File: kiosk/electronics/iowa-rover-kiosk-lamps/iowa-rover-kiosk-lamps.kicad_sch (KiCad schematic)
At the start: 12 parts, among them J1 Conn_01x08, SW1 SW_Push, U1 TPIC6A595NE

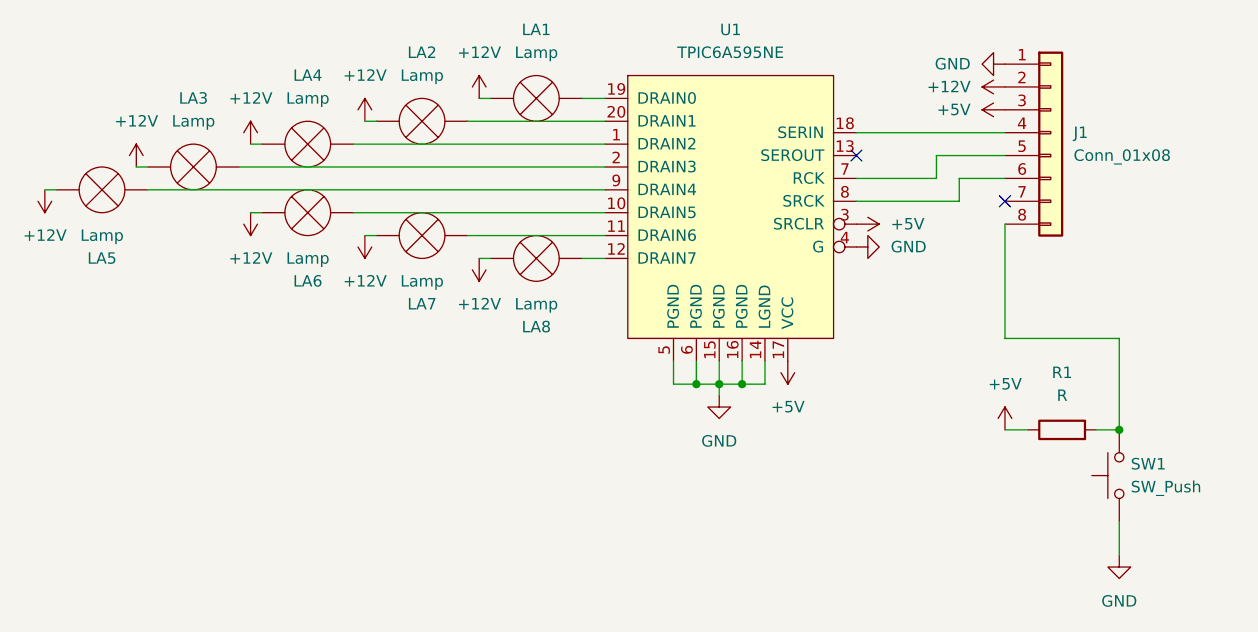
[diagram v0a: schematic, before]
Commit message: initial pass at board drawings
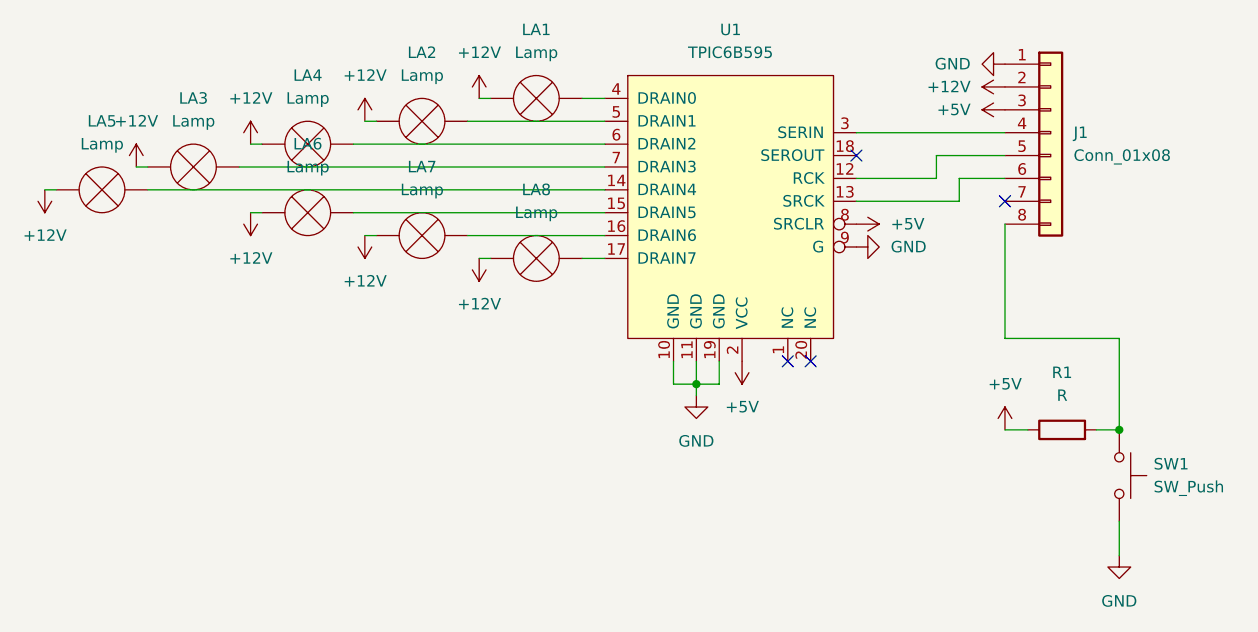
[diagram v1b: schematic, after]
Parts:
- removed U1: TPIC6A595NE, symbol SMM:TPIC6A595NE
- added U1: TPIC6B595, Package_DIP:DIP-20_W7.62mm_Socket, symbol SMM:TPIC6B595
- J1: footprint (none) -> Connector_PinHeader_2.54mm:PinHeader_2x04_P2.54mm_Vertical
- LA1, LA2, LA3, LA4, LA5, LA6, LA7, LA8, SW1: footprint (none) -> SMM:TerminalBlock-2_P5.08mm_small
- R1: footprint (none) -> SMM:Resistor_L6.3mm_D2.5mm_P10.16mm_Horizontal
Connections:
- net +12V: now also LA1.1 (-), LA2.1 (-), LA3.1 (-), LA4.1 (-), LA5.1 (-), LA6.1 (-), LA7.1 (-), LA8.1 (-); no longer LA1.2 (+), LA2.2 (+), LA3.2 (+), LA4.2 (+), LA5.2 (+), LA6.2 (+), LA7.2 (+), LA8.2 (+)
- net +5V: now also U1.2 (VCC), U1.8 (SRCLR)
- net GND: now also SW1.2, U1.10 (GND), U1.11 (GND), U1.19 (GND), U1.9 (G); no longer SW1.1
- net at J1.4 (Pin_4): now also U1.3 (SERIN)
- net at J1.5 (Pin_5): now also U1.12 (RCK)
- net at J1.6 (Pin_6): now also U1.13 (SRCK)
- net at J1.8 (Pin_8), R1.2: now also SW1.1; no longer SW1.2
- new net: LA7.2 (+), U1.16 (DRAIN6)
- new net: LA6.2 (+), U1.15 (DRAIN5)
- new net: LA5.2 (+), U1.14 (DRAIN4)
- new net: LA8.2 (+), U1.17 (DRAIN7)
- new net: LA1.2 (+), U1.4 (DRAIN0)
- new net: LA2.2 (+), U1.5 (DRAIN1)
- new net: LA4.2 (+), U1.6 (DRAIN2)
- new net: LA3.2 (+), U1.7 (DRAIN3)
- no-connect marks 2 -> 4
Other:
- moved on the sheet: LA1, LA2, LA3, LA4, LA5, LA6, LA7, LA8, SW1

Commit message: update
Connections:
- net +12V: no longer LA8.1 (-)
- net +5V: now also LA8.1 (-)
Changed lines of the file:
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@@
     )
   )
-  (symbol (lib_id "power:+12V") (at 97.79 86.36 0) (unit 1)
-    (in_bom yes) (on_board yes) (dnp no) (fields_autoplaced)
-    (property "Reference" "#PWR013" (at 97.79 90.17 0)
-      (effects (font (size 1.27 1.27)) hide)
-    )
-    (property "Value" "+12V" (at 97.79 81.28 0)
-      (effects (font (size 1.27 1.27)))
-    )
-    (property "Footprint" "" (at 97.79 86.36 0)
-      (effects (font (size 1.27 1.27)) hide)
-    )
-    (property "Datasheet" "" (at 97.79 86.36 0)
-      (effects (font (size 1.27 1.27)) hide)
-    )
-    (pin "1")
-    (instances
-      (project "iowa-rover-kiosk-lamps"
-        (path "/1cdfebc0-86ff-42b6-85e4-f0a5de6890ba"
-          (reference "#PWR013") (unit 1)
+  (symbol (lib_id "power:+12V") (at 110.49 83.82 0) (unit 1)
+    (in_bom yes) (on_board yes) (dnp no) (fields_autoplaced)
+    (property "Reference" "#PWR011" (at 110.49 87.63 0)
+      (effects (font (size 1.27 1.27)) hide)
+    )
+    (property "Value" "+12V" (at 110.49 78.74 0)
+      (effects (font (size 1.27 1.27)))
+    )
+    (property "Footprint" "" (at 110.49 83.82 0)
+      (effects (font (size 1.27 1.27)) hide)
+    )
+    (property "Datasheet" "" (at 110.49 83.82 0)
+      (effects (font (size 1.27 1.27)) hide)
+    )
+    (pin "1")
+    (instances
+      (project "iowa-rover-kiosk-lamps"
+        (path "/1cdfebc0-86ff-42b6-85e4-f0a5de6890ba"
+          (reference "#PWR011") (unit 1)
+        )
+      )
+    )
+  )
+  (symbol (lib_id "power:+12V") (at 123.19 81.28 0) (unit 1)
+    (in_bom yes) (on_board yes) (dnp no) (fields_autoplaced)
+    (property "Reference" "#PWR010" (at 123.19 85.09 0)
+      (effects (font (size 1.27 1.27)) hide)
+    )
+    (property "Value" "+12V" (at 123.19 76.2 0)
+      (effects (font (size 1.27 1.27)))
+    )
+    (property "Footprint" "" (at 123.19 81.28 0)
+      (effects (font (size 1.27 1.27)) hide)
+    )
+    (property "Datasheet" "" (at 123.19 81.28 0)
+      (effects (font (size 1.27 1.27)) hide)
+    )
+    (pin "1")
+    (instances
+      (project "iowa-rover-kiosk-lamps"
+        (path "/1cdfebc0-86ff-42b6-85e4-f0a5de6890ba"
+          (reference "#PWR010") (unit 1)
         )
       )
@@
     )
   )
+  (symbol (lib_id "power:+12V") (at 85.09 88.9 0) (unit 1)
+    (in_bom yes) (on_board yes) (dnp no) (fields_autoplaced)
+    (property "Reference" "#PWR013" (at 85.09 92.71 0)
+      (effects (font (size 1.27 1.27)) hide)
+    )
+    (property "Value" "+12V" (at 85.09 83.82 0)
+      (effects (font (size 1.27 1.27)))
+    )
+    (property "Footprint" "" (at 85.09 88.9 0)
+      (effects (font (size 1.27 1.27)) hide)
+    )
+    (property "Datasheet" "" (at 85.09 88.9 0)
+      (effects (font (size 1.27 1.27)) hide)
+    )
+    (pin "1")
+    (instances
+      (project "iowa-rover-kiosk-lamps"
+        (path "/1cdfebc0-86ff-42b6-85e4-f0a5de6890ba"
+          (reference "#PWR013") (unit 1)
+        )
+      )
+    )
+  )
   (symbol (lib_id "power:+12V") (at 97.79 93.98 0) (mirror x) (unit 1)
     (in_bom yes) (on_board yes) (dnp no) (fields_autoplaced)
@@
         (path "/1cdfebc0-86ff-42b6-85e4-f0a5de6890ba"
           (reference "#PWR015") (unit 1)
-        )
-      )
-    )
-  )
-  (symbol (lib_id "power:+12V") (at 123.19 81.28 0) (unit 1)
-    (in_bom yes) (on_board yes) (dnp no) (fields_autoplaced)
-    (property "Reference" "#PWR010" (at 123.19 85.09 0)
-      (effects (font (size 1.27 1.27)) hide)
-    )
-    (property "Value" "+12V" (at 123.19 76.2 0)
-      (effects (font (size 1.27 1.27)))
-    )
-    (property "Footprint" "" (at 123.19 81.28 0)
-      (effects (font (size 1.27 1.27)) hide)
-    )
-    (property "Datasheet" "" (at 123.19 81.28 0)
-      (effects (font (size 1.27 1.27)) hide)
-    )
-    (pin "1")
-    (instances
-      (project "iowa-rover-kiosk-lamps"
-        (path "/1cdfebc0-86ff-42b6-85e4-f0a5de6890ba"
-          (reference "#PWR010") (unit 1)
         )
       )
@@
     )
   )
+  (symbol (lib_id "power:+12V") (at 97.79 86.36 0) (unit 1)
+    (in_bom yes) (on_board yes) (dnp no) (fields_autoplaced)
+    (property "Reference" "#PWR012" (at 97.79 90.17 0)
+      (effects (font (size 1.27 1.27)) hide)
+    )
+    (property "Value" "+12V" (at 97.79 81.28 0)
+      (effects (font (size 1.27 1.27)))
+    )
+    (property "Footprint" "" (at 97.79 86.36 0)
+      (effects (font (size 1.27 1.27)) hide)
+    )
+    (property "Datasheet" "" (at 97.79 86.36 0)
+      (effects (font (size 1.27 1.27)) hide)
+    )
+    (pin "1")
+    (instances
+      (project "iowa-rover-kiosk-lamps"
+        (path "/1cdfebc0-86ff-42b6-85e4-f0a5de6890ba"
+          (reference "#PWR012") (unit 1)
+        )
+      )
+    )
+  )
   (symbol (lib_id "power:+12V") (at 181.61 80.01 90) (unit 1)
     (in_bom yes) (on_board yes) (dnp no) (fields_autoplaced)
@@
     )
   )
-  (symbol (lib_id "power:+12V") (at 85.09 88.9 0) (unit 1)
-    (in_bom yes) (on_board yes) (dnp no) (fields_autoplaced)
-    (property "Reference" "#PWR012" (at 85.09 92.71 0)
-      (effects (font (size 1.27 1.27)) hide)
-    )
-    (property "Value" "+12V" (at 85.09 83.82 0)
-      (effects (font (size 1.27 1.27)))
-    )
-    (property "Footprint" "" (at 85.09 88.9 0)
-      (effects (font (size 1.27 1.27)) hide)
-    )
-    (property "Datasheet" "" (at 85.09 88.9 0)
-      (effects (font (size 1.27 1.27)) hide)
-    )
-    (pin "1")
-    (instances
-      (project "iowa-rover-kiosk-lamps"
-        (path "/1cdfebc0-86ff-42b6-85e4-f0a5de6890ba"
-          (reference "#PWR012") (unit 1)
-        )
-      )
-    )
-  )
   (symbol (lib_id "power:+12V") (at 74.93 91.44 0) (mirror x) (unit 1)
     (in_bom yes) (on_board yes) (dnp no) (fields_autoplaced)
@@
         (path "/1cdfebc0-86ff-42b6-85e4-f0a5de6890ba"
           (reference "#PWR014") (unit 1)
-        )
-      )
-    )
-  )
-  (symbol (lib_id "power:+12V") (at 123.19 99.06 0) (mirror x) (unit 1)
-    (in_bom yes) (on_board yes) (dnp no) (fields_autoplaced)
-    (property "Reference" "#PWR017" (at 123.19 95.25 0)
-      (effects (font (size 1.27 1.27)) hide)
-    )
-    (property "Value" "+12V" (at 123.19 104.14 0)
-      (effects (font (size 1.27 1.27)))
-    )
-    (property "Footprint" "" (at 123.19 99.06 0)
-      (effects (font (size 1.27 1.27)) hide)
-    )
-    (property "Datasheet" "" (at 123.19 99.06 0)
-      (effects (font (size 1.27 1.27)) hide)
-    )
-    (pin "1")
-    (instances
-      (project "iowa-rover-kiosk-lamps"
-        (path "/1cdfebc0-86ff-42b6-85e4-f0a5de6890ba"
-          (reference "#PWR017") (unit 1)
-        )
-      )
-    )
-  )
-  (symbol (lib_id "power:+12V") (at 110.49 83.82 0) (unit 1)
-    (in_bom yes) (on_board yes) (dnp no) (fields_autoplaced)
-    (property "Reference" "#PWR011" (at 110.49 87.63 0)
-      (effects (font (size 1.27 1.27)) hide)
-    )
-    (property "Value" "+12V" (at 110.49 78.74 0)
-      (effects (font (size 1.27 1.27)))
-    )
-    (property "Footprint" "" (at 110.49 83.82 0)
-      (effects (font (size 1.27 1.27)) hide)
-    )
-    (property "Datasheet" "" (at 110.49 83.82 0)
-      (effects (font (size 1.27 1.27)) hide)
-    )
-    (pin "1")
-    (instances
-      (project "iowa-rover-kiosk-lamps"
-        (path "/1cdfebc0-86ff-42b6-85e4-f0a5de6890ba"
-          (reference "#PWR011") (unit 1)
         )
       )
@@
         )
       )
+    )
+  )
+  (symbol (lib_id "power:+5V") (at 123.19 99.06 180) (unit 1)
+    (in_bom yes) (on_board yes) (dnp no) (fields_autoplaced)
+    (property "Reference" "#PWR017" (at 123.19 95.25 0)
+      (effects (font (size 1.27 1.27)) hide)
+    )
+    (property "Value" "+5V" (at 123.19 104.14 0)
+      (effects (font (size 1.27 1.27)))
+    )
+    (property "Footprint" "" (at 123.19 99.06 0)
+      (effects (font (size 1.27 1.27)) hide)
+    )
+    (property "Datasheet" "" (at 123.19 99.06 0)
+      (effects (font (size 1.27 1.27)) hide)
+    )
+    (pin "1")
+    (instances
+      (project "iowa-rover-kiosk-lamps"
+        (path "/1cdfebc0-86ff-42b6-85e4-f0a5de6890ba"
+          (reference "#PWR017") (unit 1)
+        )
+      )

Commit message: add pdf schematics
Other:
- company: (none) -> Science Museum of Minnesota
- title: (none) -> Iowa Science Rover Kiosk - Lamps Board
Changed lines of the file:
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@@
 (kicad_sch (version 20230121) (generator eeschema)
   (paper "A4")
+  (title_block
+    (title "Iowa Science Rover Kiosk - Lamps Board")
+    (date "2023-10-05")
+    (rev "0")
+    (company "Science Museum of Minnesota")
+    (comment 1 "Kate Swanson")
+  )
   (junction (at 147.32 113.03) (diameter 0) (color 0 0 0 0)
   )
